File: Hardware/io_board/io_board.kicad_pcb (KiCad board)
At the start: 2 copper layers, 80.8 x 60.1 mm, 36 parts, among them J1 Conn_01x40, J2 Conn_02x05_Odd_Even, J3 Mini-DIN-6, J4 Conn_02x10_Odd_Even, U1 74LS138, U2 W65C22NxP, U3 74LS14

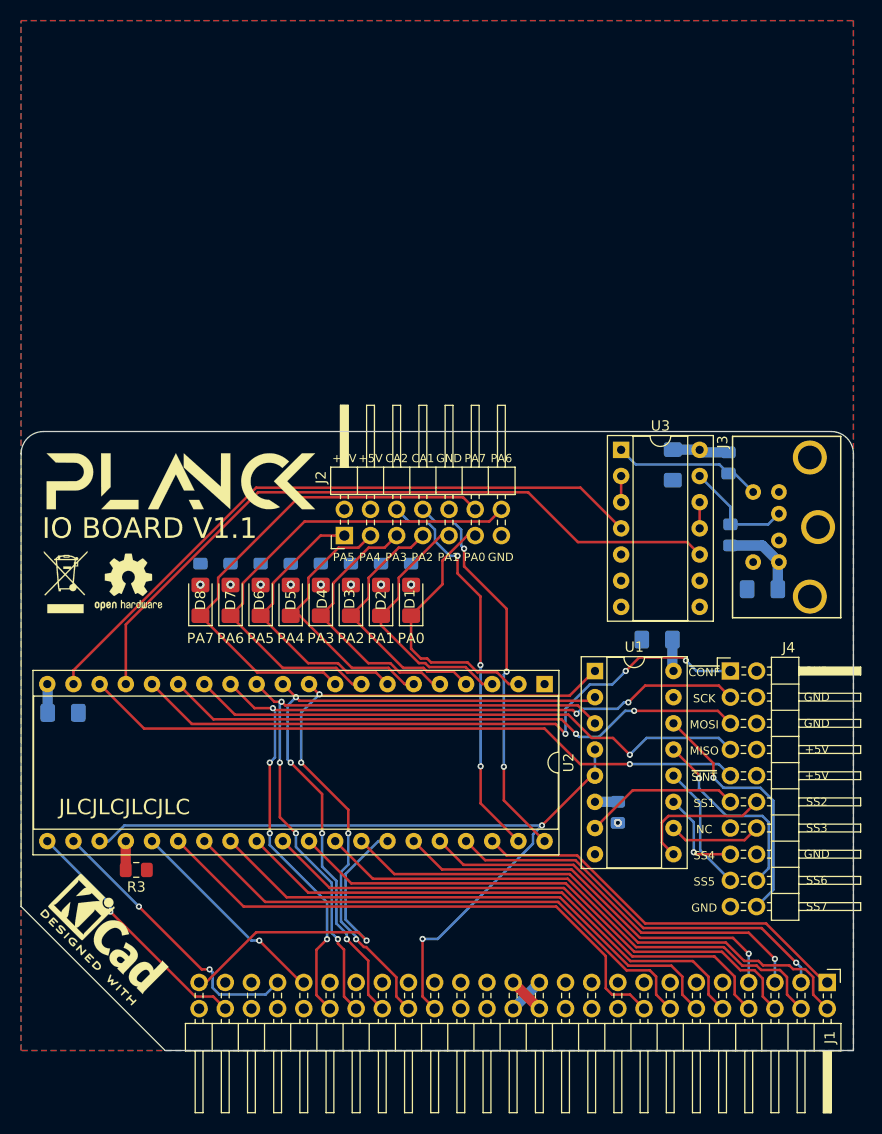
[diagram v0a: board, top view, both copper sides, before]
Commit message: Make IO board through hole
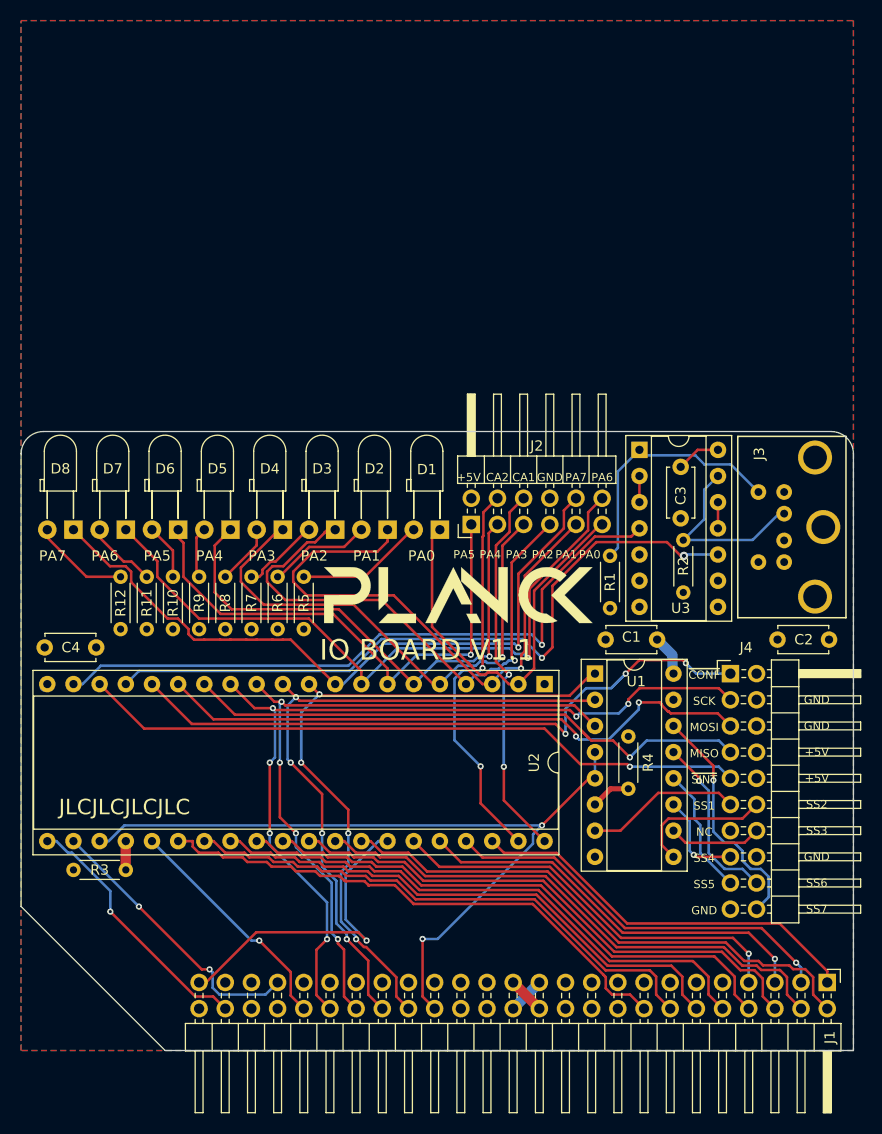
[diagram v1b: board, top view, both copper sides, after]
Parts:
- removed the G*** at (29.3, -55.8)
- removed the G*** at (15.5, -55.2)
- removed REF**: OSHW-Logo2_7.3x6mm_SilkScreen, Symbol:OSHW-Logo2_7.3x6mm_SilkScreen
- removed REF**: WEEE-Logo_4.2x6mm_SilkScreen, Symbol:WEEE-Logo_4.2x6mm_SilkScreen
- removed REF**: KiCad-Logo2_5mm_SilkScreen, Symbol:KiCad-Logo2_5mm_SilkScreen
- added G***: LOGO, Logo:logo, F.Cu at (42.4, -44.2)
- C1, C2, C3, C4: value C_Small -> 4.7u; footprint Capacitor_SMD:C_1206_3216Metric_Pad1.42x1.75mm_HandSolder -> Capacitor_THT:C_Disc_D4.7mm_W2.5mm_P5.00mm; moved to F.Cu
- D1, D2, D3, D4, D5, D6, D7, D8: footprint LED_SMD:LED_1206_3216Metric_Pad1.42x1.75mm_HandSolder -> LED_THT:LED_D3.0mm_Horizontal_O3.81mm_Z2.0mm
- J2: value Conn_02x05_Odd_Even -> Conn_02x06_Odd_Even; footprint Connector_PinHeader_2.54mm:PinHeader_2x07_P2.54mm_Horizontal -> Connector_PinHeader_2.54mm:PinHeader_2x06_P2.54mm_Horizontal
- R1, R10, R11, R12, R2, R4, R5, R6, R7, R8, R9: footprint Resistor_SMD:R_0805_2012Metric_Pad1.15x1.40mm_HandSolder -> Resistor_THT:R_Axial_DIN0204_L3.6mm_D1.6mm_P5.08mm_Horizontal; moved to F.Cu
- R3: footprint Resistor_SMD:R_0805_2012Metric_Pad1.15x1.40mm_HandSolder -> Resistor_THT:R_Axial_DIN0204_L3.6mm_D1.6mm_P5.08mm_Horizontal
- moved R1 18.2 mm to (57.1, -42.9), turned to 90 degrees
- moved D8 14.1 mm to (5.08, -50.5), turned to 180 degrees
- moved J2 12.4 mm to (43.7, -51.1)
- moved D7 12.3 mm to (10.2, -50.5), turned to 180 degrees
- moved D6 10.5 mm to (15.2, -50.5), turned to 180 degrees
- moved R5 10.4 mm to (27.4, -46.0), turned to 270 degrees
- moved R6 10.0 mm to (24.9, -46.0), turned to 270 degrees
- moved R7 9.66 mm to (22.4, -46.0), turned to 270 degrees
- moved R8 9.27 mm to (19.8, -46.0), turned to 270 degrees
- moved D5 9.01 mm to (20.3, -50.5), turned to 180 degrees
- moved R9 8.89 mm to (17.3, -46.0), turned to 270 degrees
- moved R10 8.51 mm to (14.7, -46.0), turned to 270 degrees
- moved R11 8.13 mm to (12.2, -46.0), turned to 270 degrees
- moved D4 7.78 mm to (25.4, -50.5), turned to 180 degrees
- moved R12 7.75 mm to (9.65, -46.0), turned to 270 degrees
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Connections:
- C2 pad 2: Net-(C2-Pad2) -> GND
- J2 pad 10: GND -> /PA7
- J2 pad 12: /PA7 -> /PA6
- J2 pad 4: +5V -> /CA2
- J2 pad 6: /CA2 -> /CA1
- J2 pad 8: /CA1 -> GND
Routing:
- net /PA1: track 25.3 -> 55.9 mm, vias 0 -> 1
- net /PA2: track 26.0 -> 54.8 mm, vias 0 -> 1
- net /PA3: track 26.3 -> 52.1 mm, vias 0 -> 1
- net /PA4: track 27.1 -> 52.7 mm, vias 0 -> 1
- net /PA5: track 27.7 -> 51.7 mm, vias 0 -> 1
- net CLK_12M: track 0.00 -> 22.8 mm, vias 0 -> 1
- net CLK: track 20.4 -> 0.00 mm, vias 1 -> 0
- net /PA6: track 47.2 -> 67.2 mm, vias 0 -> 1
- net /PA7: track 48.9 -> 68.9 mm, vias 0 -> 1
- net /PA0: track 26.5 -> 40.7 mm
- net Net-(D1-Pad2): track 0.00 -> 12.6 mm, vias 1 -> 0
- net +5V: track 23.0 -> 12.3 mm, vias 1 -> 0
- net Net-(J3-Pad5): track 14.5 -> 24.7 mm
- net Net-(D2-Pad2): track 0.00 -> 10.0 mm, vias 1 -> 0
- net Net-(D8-Pad2): track 0.00 -> 9.45 mm, vias 1 -> 0
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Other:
- rule pad_to_mask_clearance: 0.05 -> 0

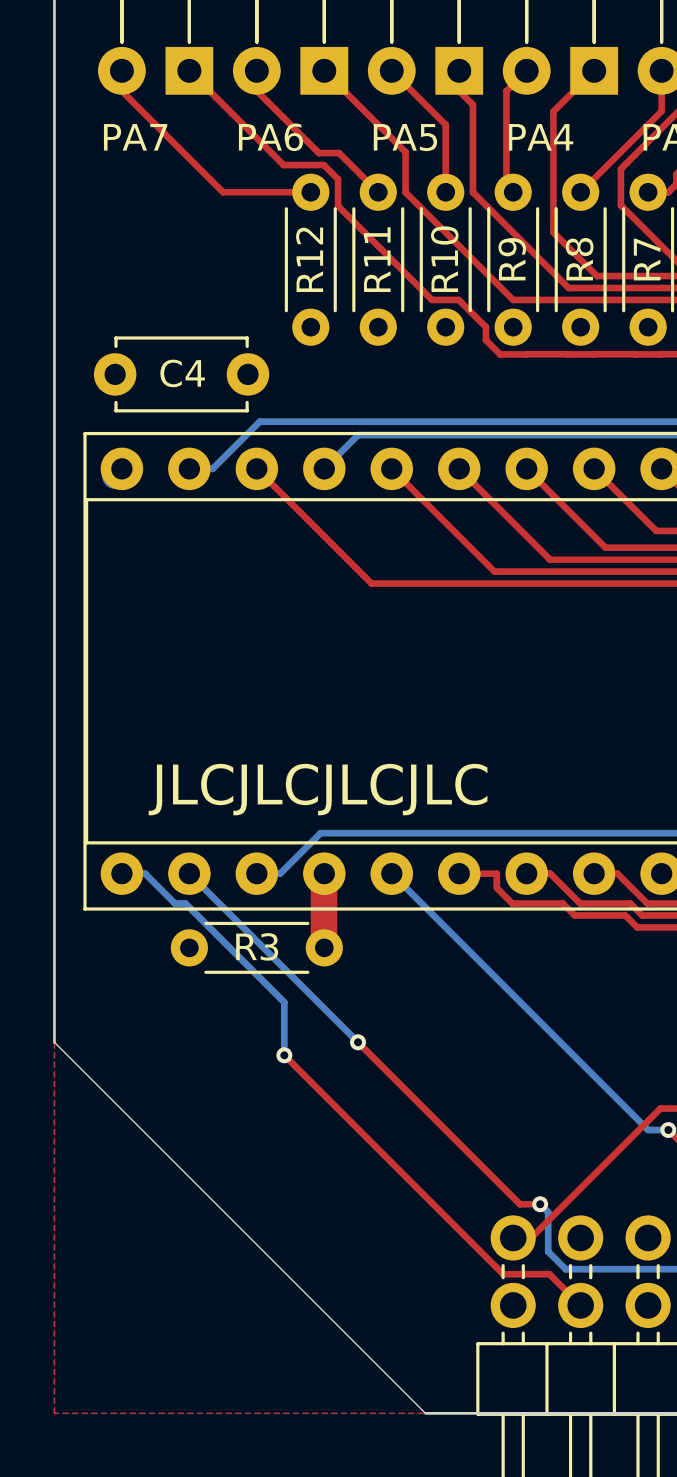
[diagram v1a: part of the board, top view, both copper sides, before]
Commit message: Add logos
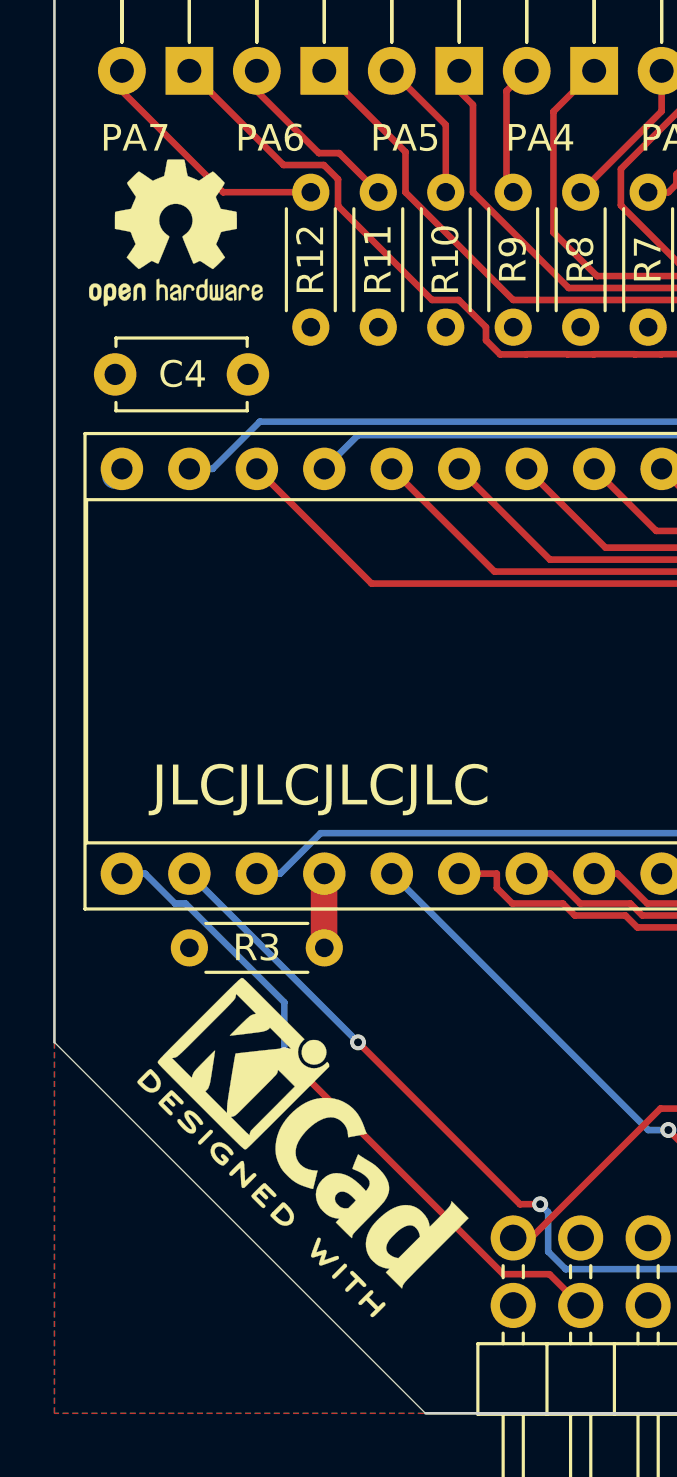
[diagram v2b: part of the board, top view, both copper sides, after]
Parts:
- added REF**: KiCad-Logo2_5mm_SilkScreen, Symbol:KiCad-Logo2_5mm_SilkScreen, F.Cu at (9.65, -10.2)
- added REF**: OSHW-Logo2_7.3x6mm_SilkScreen, Symbol:OSHW-Logo2_7.3x6mm_SilkScreen, F.Cu at (4.57, -44.5)

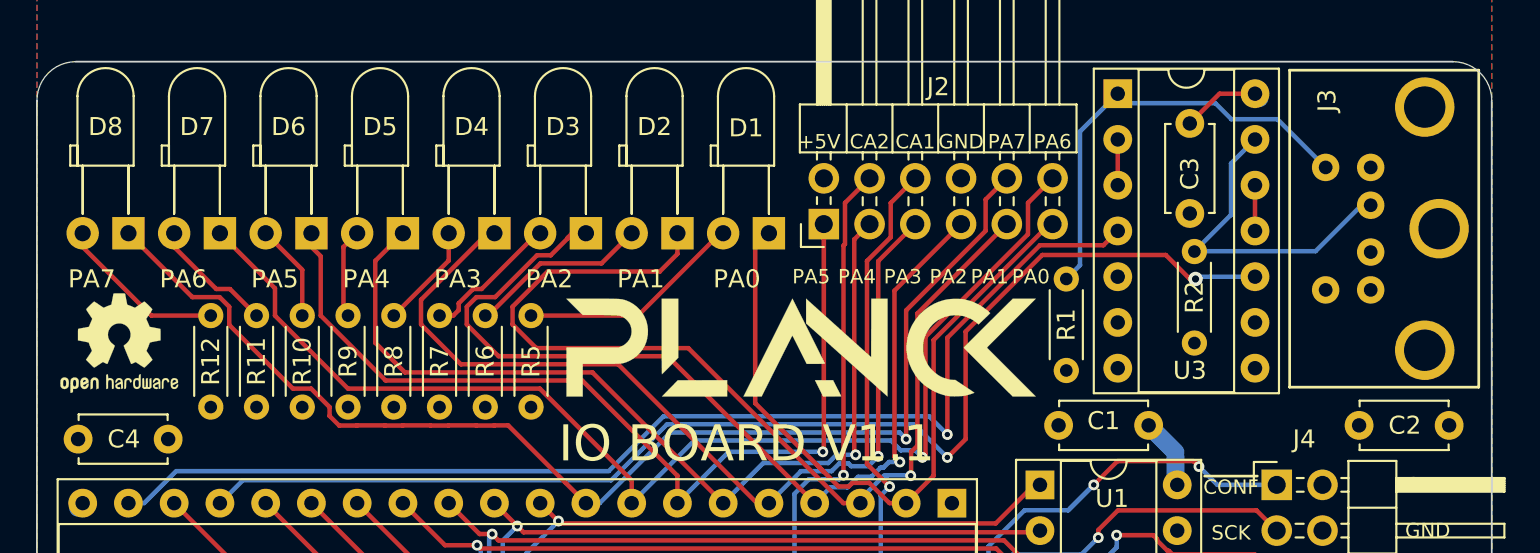
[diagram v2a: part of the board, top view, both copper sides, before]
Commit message: final update for through hole conversion
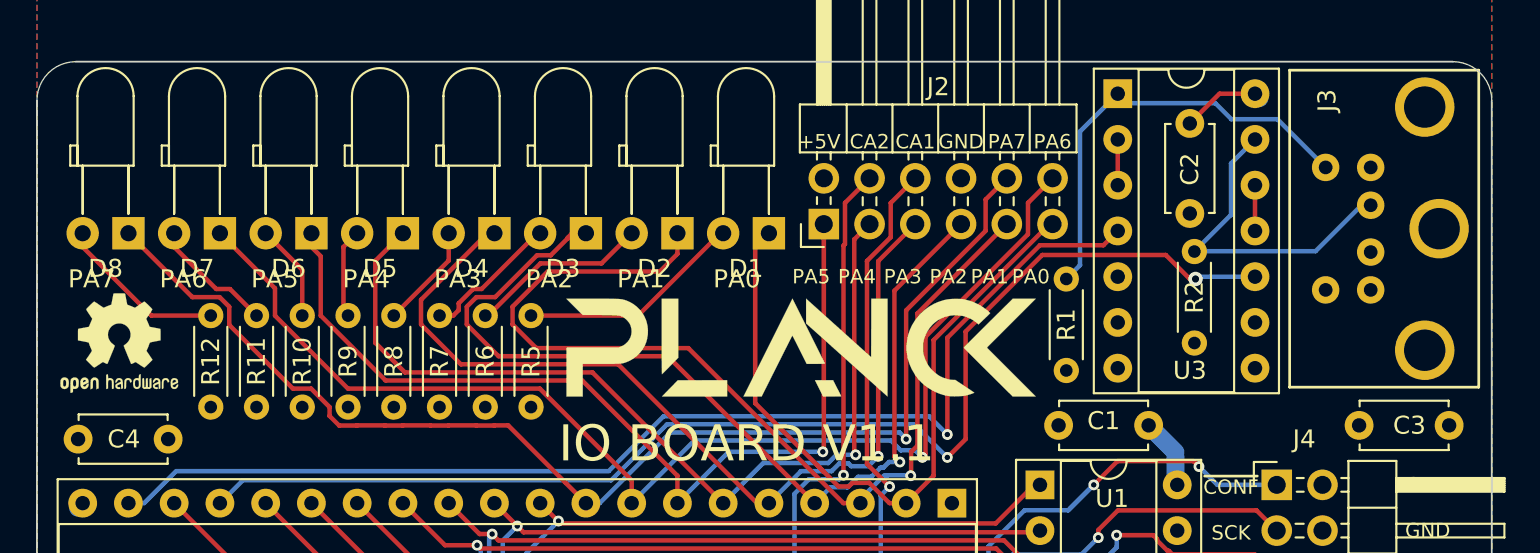
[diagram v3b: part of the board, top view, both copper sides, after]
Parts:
- C1, C2, C4: value 4.7u -> 10n
- C3: value 4.7u -> 100n
- D1, D2, D3, D4, D5, D6, D7, D8: footprint LED_THT:LED_D3.0mm_Horizontal_O3.81mm_Z2.0mm -> LED_THT:LED_D3.0mm_Horizontal_O3.81mm_Z6.0mm
- moved C2 19.2 mm to (64.0, -56.6), turned to 270 degrees
- moved C3 19.2 mm to (73.4, -39.9), turned to 0 degrees
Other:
- board text added: "© Jonathan Foucher 2021"
- board text removed: "KB / SPI / IO BOARD V1.1"

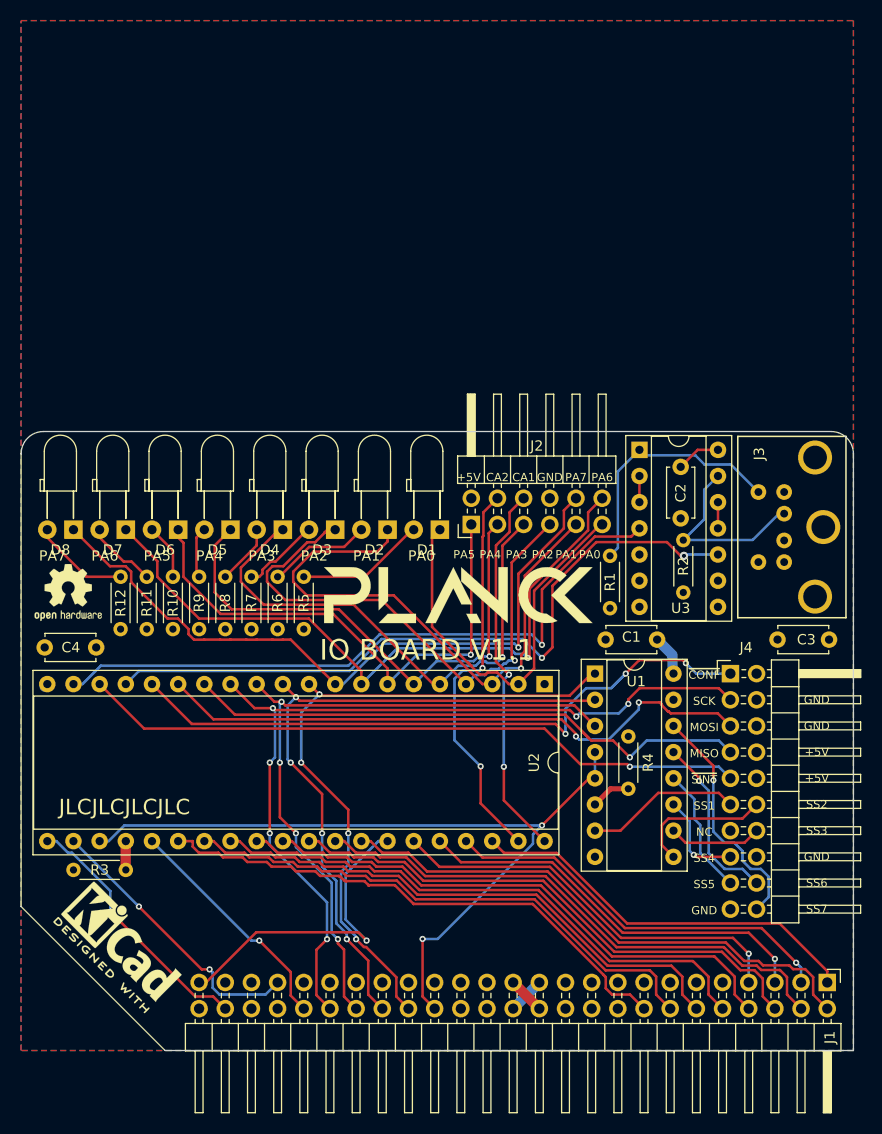
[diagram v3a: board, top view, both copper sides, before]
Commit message: update io board with bigger resistors
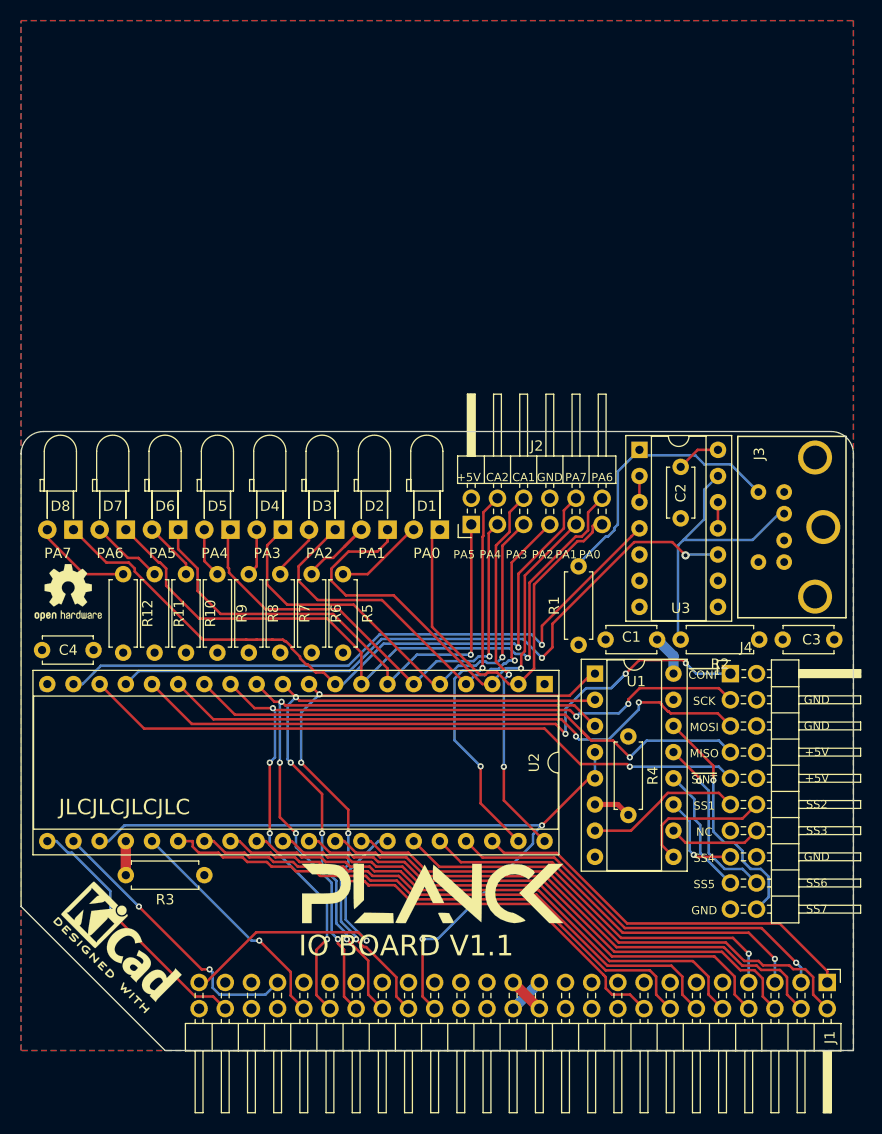
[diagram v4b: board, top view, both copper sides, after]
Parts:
- removed the G*** at (42.4, -44.2)
- added G***: LOGO, Logo:logo-sm, F.Cu at (39.9, -15.2)
- R1, R10, R11, R12, R2, R3, R4, R5, R6, R7, R8, R9: footprint Resistor_THT:R_Axial_DIN0204_L3.6mm_D1.6mm_P5.08mm_Horizontal -> Resistor_THT:R_Axial_DIN0207_L6.3mm_D2.5mm_P7.62mm_Horizontal
- moved R3 12.7 mm to (17.8, -17.0), turned to 180 degrees
- moved R2 8.67 mm to (71.6, -39.9), turned to 180 degrees
- moved R1 4.68 mm to (54.1, -39.4)
- moved R5 3.82 mm to (31.2, -46.2)
- moved R6 3.31 mm to (28.2, -46.2)
- moved R7 2.81 mm to (25.1, -46.2)
- moved R8 2.30 mm to (22.1, -46.2)
- moved R9 1.80 mm to (19.1, -46.2)
- moved R10 1.30 mm to (16.0, -46.2)
- moved R11 0.80 mm to (13.0, -46.2)
- moved C3 0.51 mm to (73.9, -39.9)
- moved R12 0.36 mm to (9.91, -46.2)
- moved C4 0.36 mm to (2.03, -38.9)
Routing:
- net PS2_DATA: track 18.3 -> 28.2 mm
- net /PA1: track 55.9 -> 48.6 mm
- net /PA2: track 54.8 -> 48.9 mm
- net Net-(D1-Pad2): track 12.6 -> 8.65 mm
- net /PA3: track 52.1 -> 48.4 mm
- net /PA4: track 52.7 -> 49.7 mm
- net Net-(J3-Pad5): track 24.7 -> 27.2 mm
- net Net-(U2-Pad17): track 68.8 -> 66.6 mm
- net Net-(U2-Pad19): track 65.2 -> 63.1 mm
- net Net-(D3-Pad2): track 7.70 -> 5.84 mm
- net /PA6: track 67.2 -> 68.6 mm
- net Net-(D4-Pad2): track 5.83 -> 4.63 mm
- net Net-(D2-Pad2): track 10.0 -> 9.24 mm
- net /PA0: track 40.7 -> 41.4 mm
- net /PA7: track 68.9 -> 68.3 mm
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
